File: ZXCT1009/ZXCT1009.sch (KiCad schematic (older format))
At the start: 3 parts

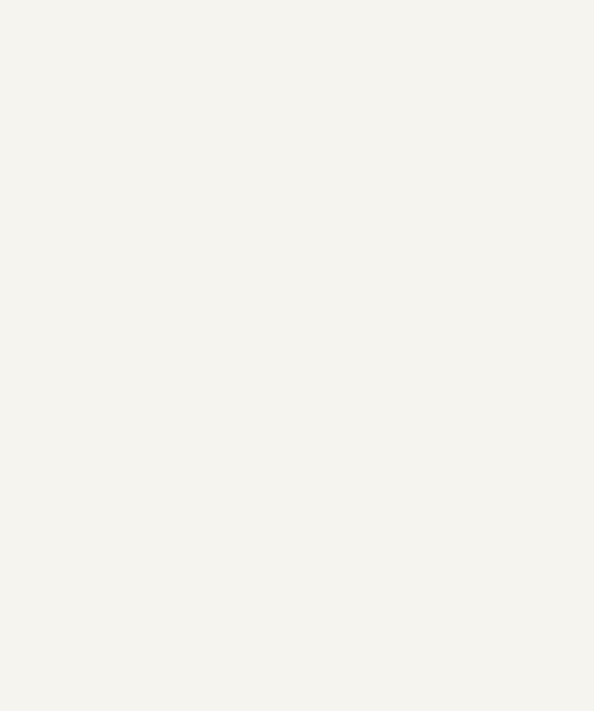
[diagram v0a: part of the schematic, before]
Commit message: adding bluepill.lib
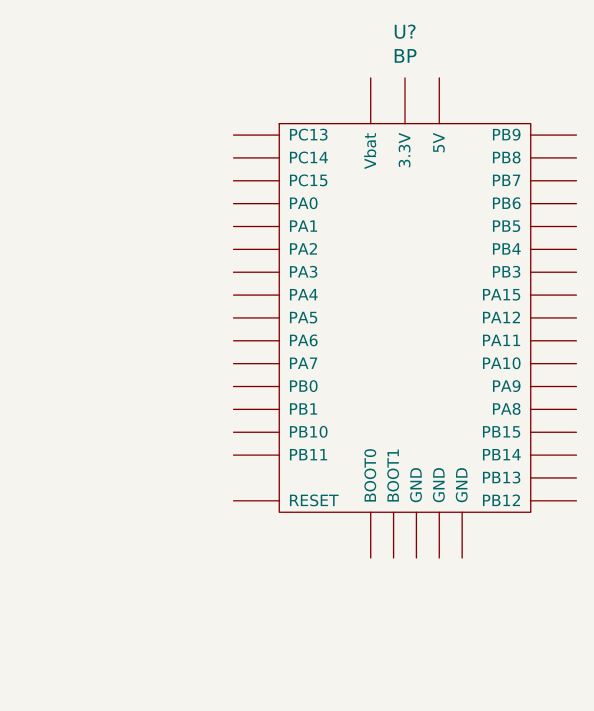
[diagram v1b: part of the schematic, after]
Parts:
- added U?: BP, symbol BP
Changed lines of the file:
@@
 LIBS:contrib
 LIBS:valves
+LIBS:bluepill
+LIBS:ZXCT1009-cache
 EELAYER 25 0
 EELAYER END
@@
 Text GLabel 4100 3650 2    60   Input ~ 0
 Vin
+$Comp
+L BP U?
+U 1 1 59BF5379
+P 8350 2150
+F 0 "U?" H 8350 3400 60  0000 C CNN
+F 1 "BP" H 8350 3294 60  0000 C CNN
+F 2 "" H 8250 2900 60  0001 C CNN
+F 3 "" H 8250 2900 60  0001 C CNN
+	1    8350 2150
+	1    0    0    -1
+$EndComp
 $EndSCHEMATC

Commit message: buat PCB, ternyata bluepill.lib tidak sesuai penomoran kakinya, felix perbaiki
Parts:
- removed R?: R_Variable, symbol R_Variable
- added R1: R, Resistors_SMD:R_0805_HandSoldering, symbol R
- R2: renamed from R?; footprint (none) -> Resistors_ThroughHole:Resistor_Horizontal_RM20mm
- U1: renamed from U?; footprint (none) -> Housings_SOT-23_SOT-143_TSOT-6:SOT-23
- U2: renamed from U?; footprint (none) -> Sockets_DIP:DIP-40__600_ELL
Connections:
- wire segments 14 -> 16
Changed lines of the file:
@@
 $EndDescr
 $Comp
-L ZXCT1009 U?
+L ZXCT1009 U1
 U 1 1 59BBFCF0
 P 5300 3450
-F 0 "U?" H 4550 4250 60  0000 C CNN
+F 0 "U1" H 4550 4250 60  0000 C CNN
 F 1 "ZXCT1009" H 4700 4150 60  0000 C CNN
-F 2 "" H 5300 3450 60  0001 C CNN
+F 2 "Housings_SOT-23_SOT-143_TSOT-6:SOT-23" H 5300 3450 60  0001 C CNN
 F 3 "" H 5300 3450 60  0001 C CNN
 	1    5300 3450
@@
 $EndComp
 $Comp
-L R R?
+L R R2
 U 1 1 59BBFF78
 P 5900 3150
-F 0 "R?" V 5980 3150 50  0000 C CNN
+F 0 "R2" V 5980 3150 50  0000 C CNN
 F 1 "R" V 5900 3150 50  0000 C CNN
-F 2 "" V 5830 3150 50  0001 C CNN
+F 2 "Resistors_ThroughHole:Resistor_Horizontal_RM20mm" V 5830 3150 50  0001 C CNN
 F 3 "" H 5900 3150 50  0001 C CNN
 	1    5900 3150
 	0    -1   -1   0
-$EndComp
-Text GLabel 5700 2700 2    60   Input ~ 0
-Vout
-$Comp
-L R_Variable R?
-U 1 1 59BC0487
-P 4050 3200
-F 0 "R?" V 4150 3100 50  0000 L CNN
-F 1 "R_Variable" V 3950 3150 50  0000 L CNN
-F 2 "" V 3980 3200 50  0001 C CNN
-F 3 "" H 4050 3200 50  0001 C CNN
-	1    4050 3200
-	1    0    0    -1
 $EndComp
 Wire Wire Line
@@
 Vin
 $Comp
-L BP U?
+L BP U2
 U 1 1 59BF5379
 P 8350 2150
-F 0 "U?" H 8350 3400 60  0000 C CNN
+F 0 "U2" H 8350 3400 60  0000 C CNN
 F 1 "BP" H 8350 3294 60  0000 C CNN
-F 2 "" H 8250 2900 60  0001 C CNN
+F 2 "Sockets_DIP:DIP-40__600_ELL" H 8250 2900 60  0001 C CNN
 F 3 "" H 8250 2900 60  0001 C CNN
 	1    8350 2150
 	1    0    0    -1
 $EndComp
+$Comp
+L R R1
+U 1 1 59BF559D
+P 4050 3200
+F 0 "R1" V 4130 3200 50  0000 C CNN
+F 1 "R" V 4050 3200 50  0000 C CNN
+F 2 "Resistors_SMD:R_0805_HandSoldering" V 3980 3200 50  0001 C CNN
+F 3 "" H 4050 3200 50  0001 C CNN
+	1    4050 3200
+	1    0    0    -1
+$EndComp
+Connection ~ 4050 3050
+Connection ~ 4050 3350
+Wire Wire Line
+	8500 3200 8500 3400
+Wire Wire Line
+	8500 3400 6300 3400
+Text Label 5700 2700 0    60   ~ 0
+Vout
+Text Label 7600 1650 2    60   ~ 0
+Vout
 $EndSCHEMATC

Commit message: adding terminal
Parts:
- added J1, J2: Screw_Terminal_1x02, Terminal_Blocks:TerminalBlock_Pheonix_MKDS1.5-2pol, symbol Screw_Terminal_1x02
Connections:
- wire segments 16 -> 18
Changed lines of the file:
@@
 EESchema Schematic File Version 2
+LIBS:ZXCT1009-rescue
 LIBS:power
 LIBS:device
@@
 	6050 3150 6300 3150
 Wire Wire Line
-	6300 2800 6300 3400
-Connection ~ 6300 3150
-Wire Wire Line
 	4500 3300 4500 3350
 Wire Wire Line
@@
 	4050 3350 4050 3650
 Wire Wire Line
-	4050 3650 4100 3650
+	4050 3650 4000 3650
 Wire Wire Line
 	4500 3150 4300 3150
@@
 Text Label 4100 2750 0    60   ~ 0
 ToLoad
-Text GLabel 4100 3650 2    60   Input ~ 0
-Vin
-$Comp
-L BP U2
-U 1 1 59BF5379
-P 8350 2150
-F 0 "U2" H 8350 3400 60  0000 C CNN
-F 1 "BP" H 8350 3294 60  0000 C CNN
-F 2 "Sockets_DIP:DIP-40__600_ELL" H 8250 2900 60  0001 C CNN
-F 3 "" H 8250 2900 60  0001 C CNN
-	1    8350 2150
-	1    0    0    -1
-$EndComp
 $Comp
 L R R1
@@
 Text Label 7600 1650 2    60   ~ 0
 Vout
+$Comp
+L BP U2
+U 1 1 59CB6E75
+P 8350 2150
+F 0 "U2" H 8350 3400 60  0000 C CNN
+F 1 "BP" H 8350 3294 60  0000 C CNN
+F 2 "Sockets_DIP:DIP-40__600_ELL" H 8250 2900 60  0001 C CNN
+F 3 "" H 8250 2900 60  0001 C CNN
+	1    8350 2150
+	1    0    0    -1
+$EndComp
+Wire Wire Line
+	8400 3200 8600 3200
+Connection ~ 8500 3200
+$Comp
+L Screw_Terminal_1x02 J1
+U 1 1 59CB7C36
+P 3800 3750
+F 0 "J1" H 3880 4092 50  0000 C CNN
+F 1 "Screw_Terminal_1x02" H 3880 4001 50  0000 C CNN
+F 2 "Terminal_Blocks:TerminalBlock_Pheonix_MKDS1.5-2pol" H 3800 3525 50  0001 C CNN
+F 3 "" H 3775 3750 50  0001 C CNN
+	1    3800 3750
+	1    0    0    -1
+$EndComp
+$Comp
+L Screw_Terminal_1x02 J2
+U 1 1 59CB7FE2
+P 9850 3750
+F 0 "J2" H 9770 3704 50  0000 R CNN
+F 1 "Screw_Terminal_1x02" H 9770 3795 50  0000 R CNN
+F 2 "Terminal_Blocks:TerminalBlock_Pheonix_MKDS1.5-2pol" H 9850 3525 50  0001 C CNN
+F 3 "" H 9825 3750 50  0001 C CNN
+	1    9850 3750
+	-1   0    0    1
+$EndComp
+Wire Wire Line
+	4000 3850 9650 3850
+Text Label 9650 3650 2    60   ~ 0
+ToLoad
+Connection ~ 6300 3850
+Connection ~ 6300 3400
+Wire Wire Line
+	6300 3150 6300 3850
+Text Label 4050 3450 0    60   ~ 0
+Vin
 $EndSCHEMATC

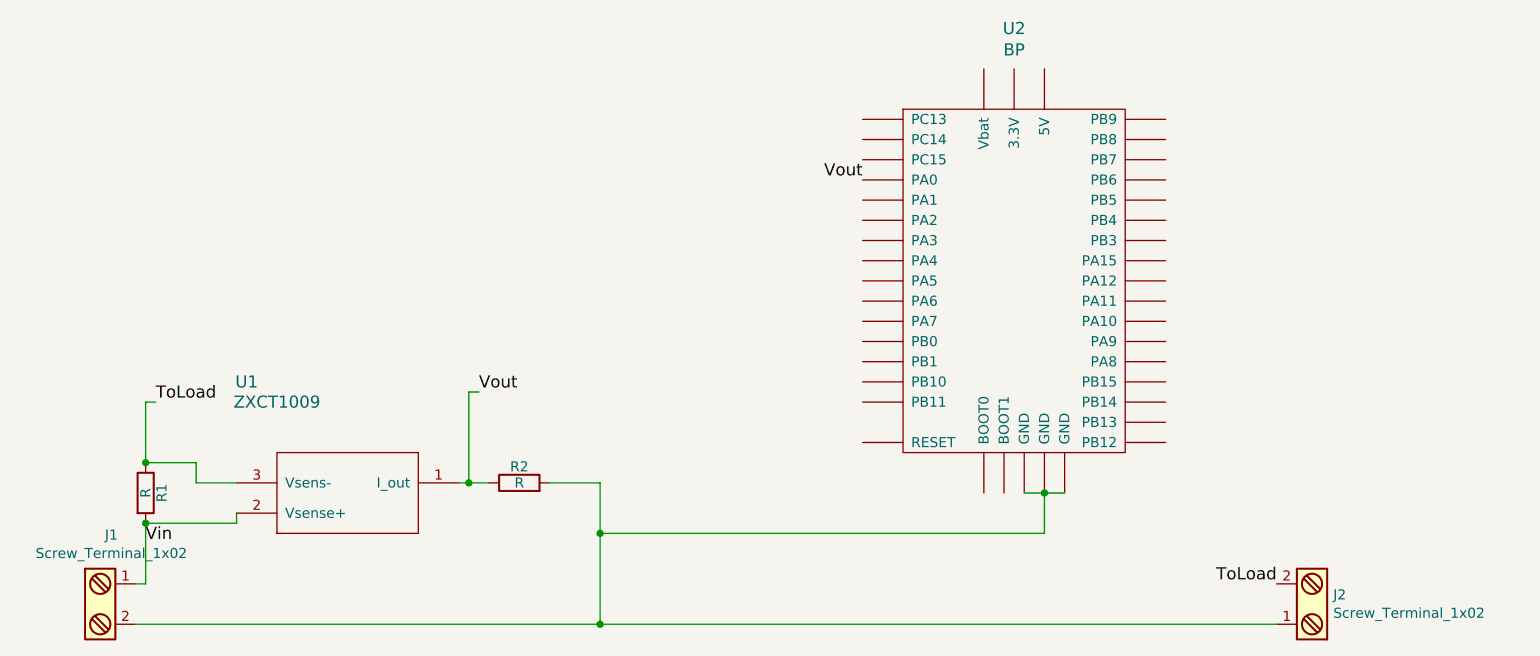
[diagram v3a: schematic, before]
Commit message: nambahkan header untuk UART dan pin lain
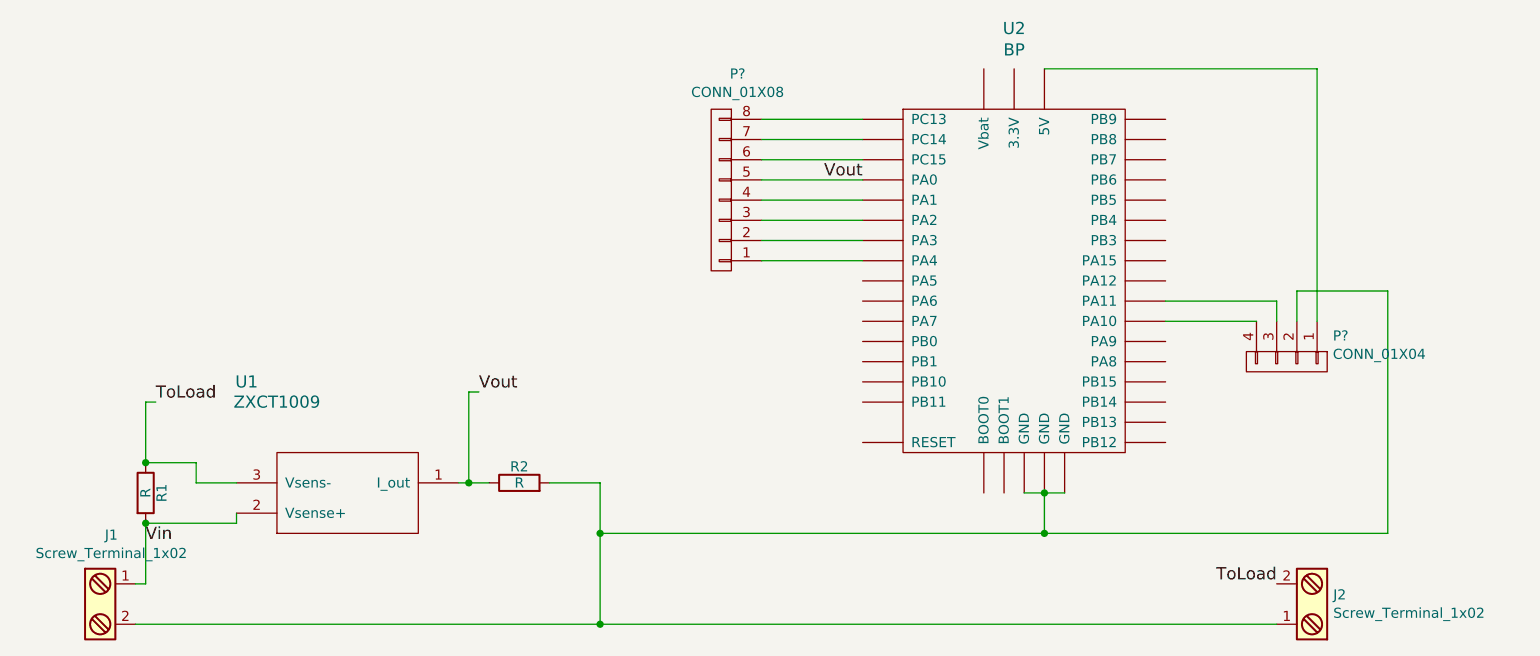
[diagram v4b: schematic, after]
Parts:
- added P?: CONN_01X04, symbol CONN_01X04
- added P?: CONN_01X08, symbol CONN_01X08
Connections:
- net Vout: now also P?.5 (P5)
- net at J1.2, J2.1, R2.2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: now also P?.2 (P2)
- net at U2.18 (5V): now also P?.1 (P1)
- net at U2.22 (PC13): now also P?.8 (P8)
- net at U2.23 (PC14): now also P?.7 (P7)
- net at U2.24 (PC15): now also P?.6 (P6)
- net at U2.26 (PA1): now also P?.4 (P4)
- net at U2.27 (PA2): now also P?.3 (P3)
- net at U2.28 (PA3): now also P?.2 (P2)
- net at U2.29 (PA4): now also P?.1 (P1)
- net at U2.7 (PA10): now also P?.4 (P4)
- net at U2.8 (PA11): now also P?.3 (P3)
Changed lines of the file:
@@
 	8500 3200 8500 3400
 Wire Wire Line
-	8500 3400 6300 3400
+	6300 3400 10200 3400
 Text Label 5700 2700 0    60   ~ 0
 Vout
@@
 Text Label 4050 3450 0    60   ~ 0
 Vin
+Wire Wire Line
+	9550 2350 9100 2350
+Wire Wire Line
+	9100 2250 9650 2250
+Wire Wire Line
+	9650 2250 9650 2350
+Connection ~ 8500 3400
+$Comp
+L CONN_01X04 P?
+U 1 1 59E57C58
+P 9700 2550
+F 0 "P?" V 9572 2778 50  0000 L CNN
+F 1 "CONN_01X04" V 9663 2778 50  0000 L CNN
+F 2 "" H 9700 2550 50  0000 C CNN
+F 3 "" H 9700 2550 50  0000 C CNN
+	1    9700 2550
+	0    1    1    0
+$EndComp
+Wire Wire Line
+	10200 3400 10200 2200
+Wire Wire Line
+	10200 2200 9750 2200
+Wire Wire Line
+	9750 2200 9750 2350
+Wire Wire Line
+	8500 1100 9850 1100
+Wire Wire Line
+	9850 1100 9850 2350
+$Comp
+L CONN_01X08 P?
+U 1 1 59E57FFD
+P 6900 1700
+F 0 "P?" H 6819 1125 50  0000 C CNN
+F 1 "CONN_01X08" H 6819 1216 50  0000 C CNN
+F 2 "" H 6900 1700 50  0000 C CNN
+F 3 "" H 6900 1700 50  0000 C CNN
+	1    6900 1700
+	-1   0    0    1
+$EndComp
+Wire Wire Line
+	7600 1350 7100 1350
+Wire Wire Line
+	7600 1450 7100 1450
+Wire Wire Line
+	7600 1550 7100 1550
+Wire Wire Line
+	7600 1650 7100 1650
+Wire Wire Line
+	7600 1750 7100 1750
+Wire Wire Line
+	7600 1850 7100 1850
+Wire Wire Line
+	7600 1950 7100 1950
+Wire Wire Line
+	7600 2050 7100 2050
 $EndSCHEMATC
